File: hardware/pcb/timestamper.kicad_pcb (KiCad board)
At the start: 2 copper layers, 75 x 100 mm, 114 parts, among them J1 Conn_Coaxial, J2 Conn_Coaxial, J3 Conn_Coaxial, J4 JTAG, J5 ISP, J6 Conn_Coaxial, J7 USB_B_Micro, U1 AP1117-33, U10 ATMEGA328-AU, U11 74HC04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

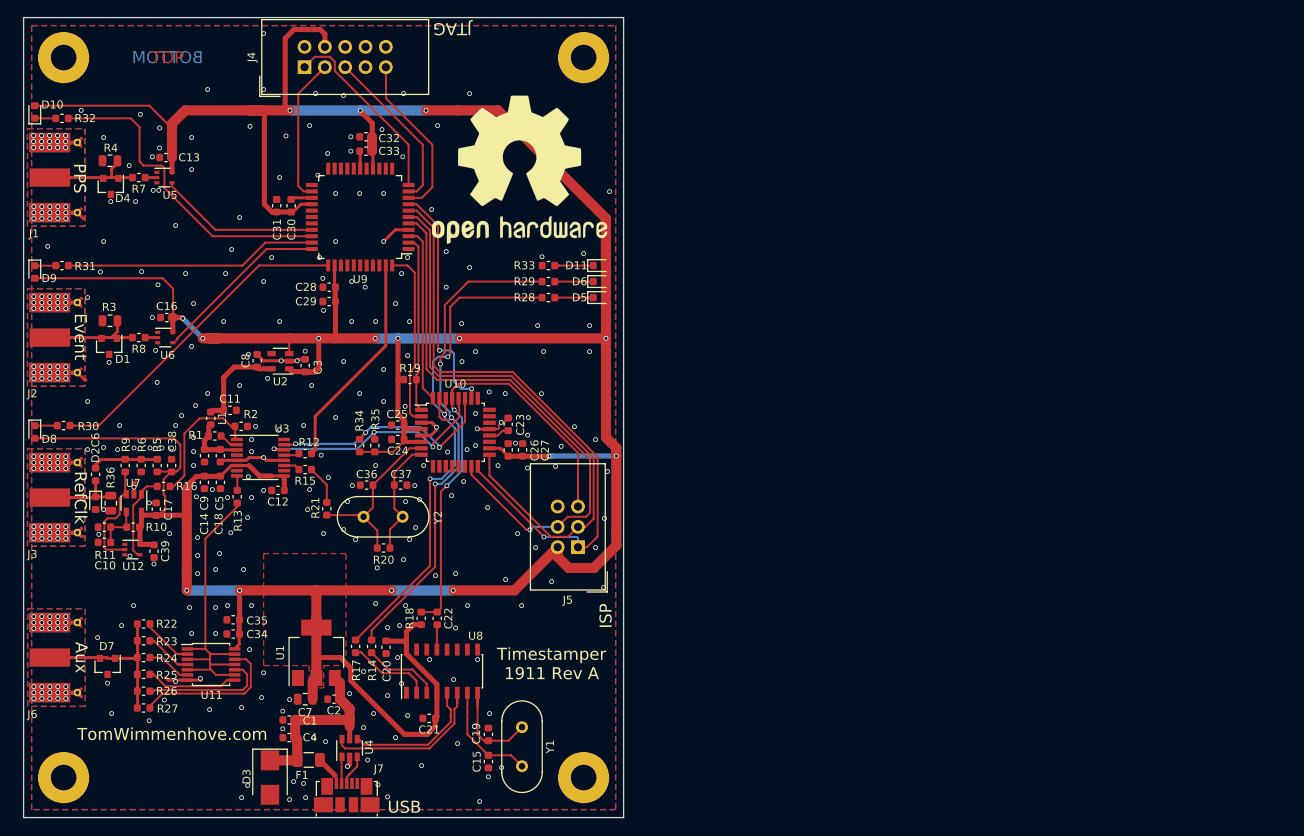
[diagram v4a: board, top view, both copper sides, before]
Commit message: Ground via insanity reduction
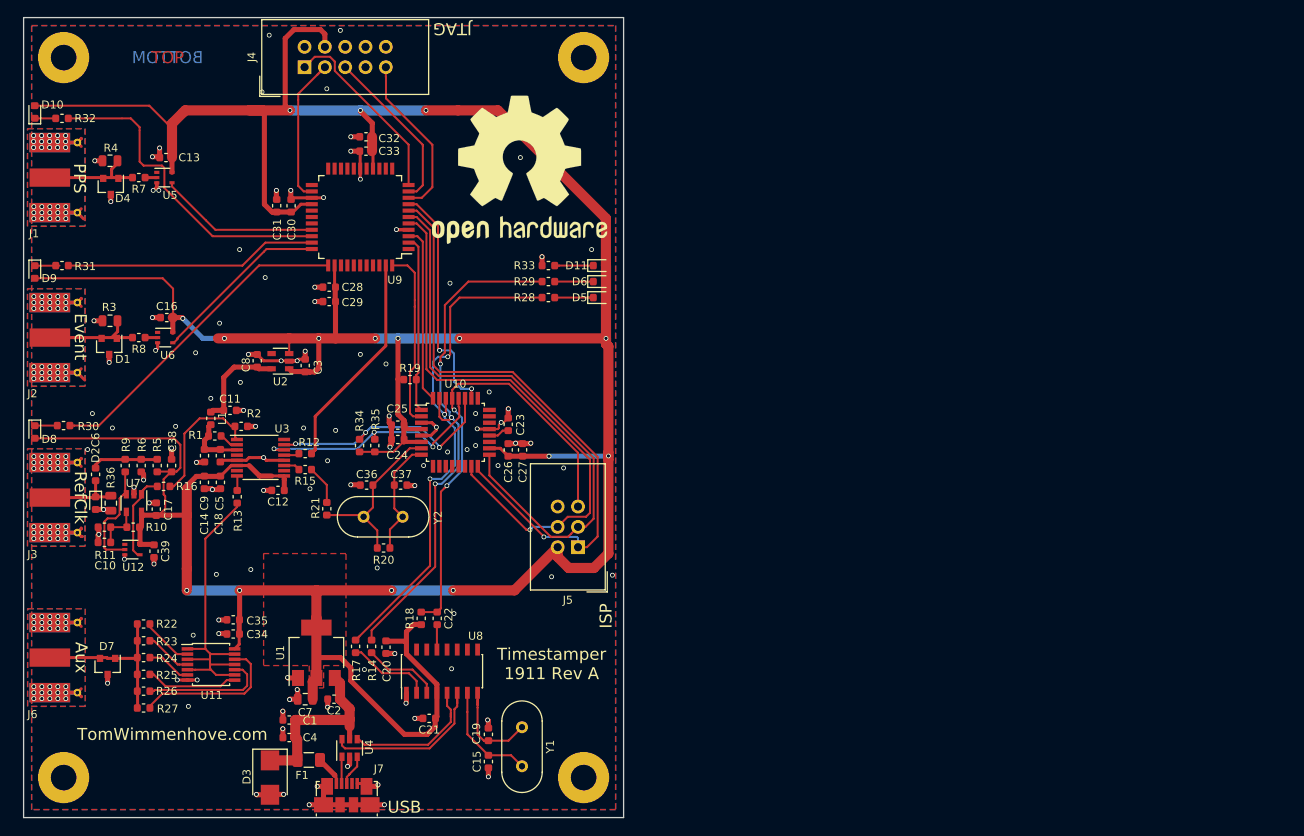
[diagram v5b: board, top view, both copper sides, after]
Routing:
- net GND: track 55.2 -> 133.9 mm, vias 371 -> 232
- net +3V3: track 516.2 -> 514.0 mm

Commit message: VCC plane on top
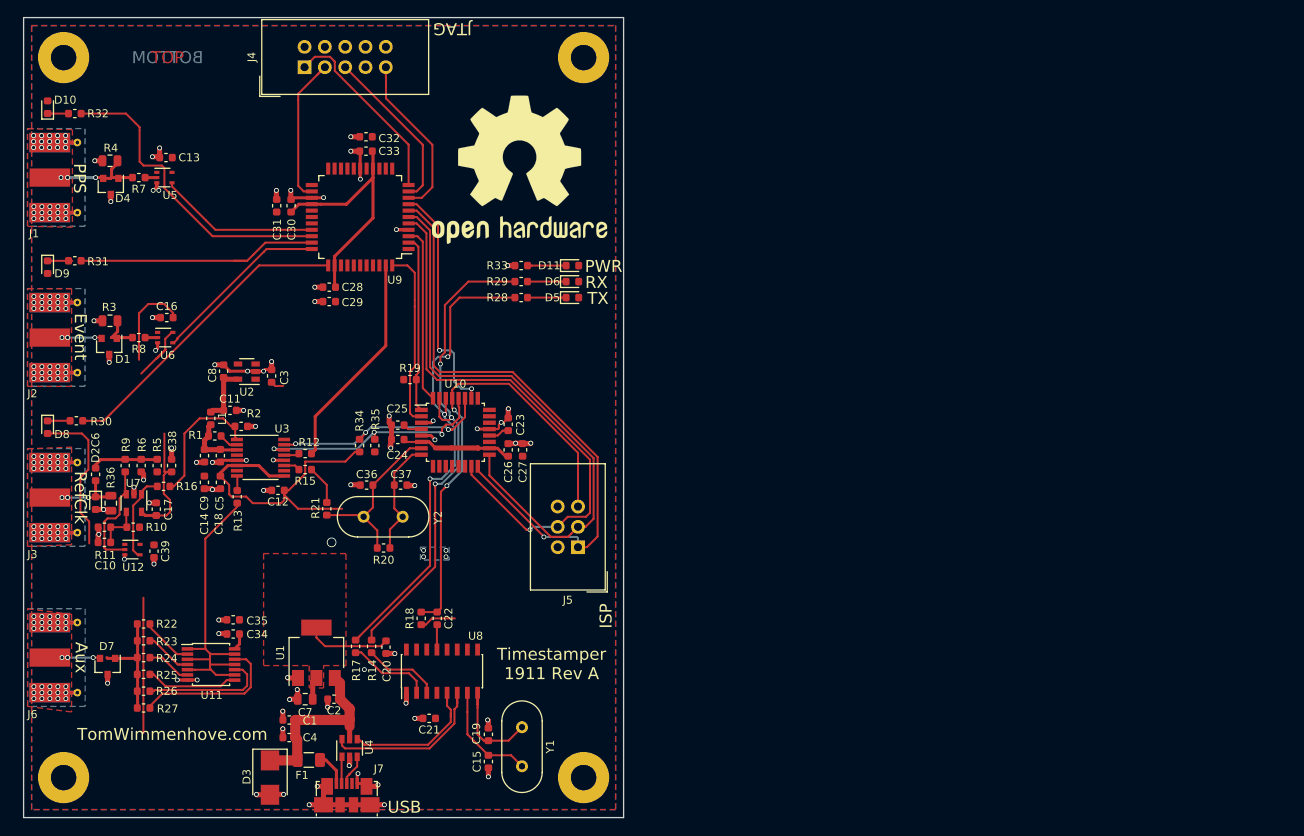
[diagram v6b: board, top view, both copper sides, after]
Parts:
- moved C3 4.40 mm to (81.0, 94.8)
- moved C8 4.40 mm to (75.0, 94.2)
- moved U2 4.40 mm to (77.9, 94.2)
- moved D11 3.40 mm to (118.6, 81.0)
- moved D5 3.40 mm to (118.6, 85.0)
- moved D6 3.40 mm to (118.6, 83.0)
- moved R28 3.40 mm to (112.2, 85.0)
- moved R29 3.40 mm to (112.2, 83.0)
- moved R33 3.40 mm to (112.2, 81.0)
- moved R32 1.71 mm to (56.4, 62.0)
- moved D10 1.71 mm to (53.0, 61.2)
- moved D8 1.71 mm to (53.0, 101.2)
- moved D9 1.71 mm to (53.0, 81.2)
- moved R30 1.71 mm to (56.6, 100.4)
- moved R31 1.71 mm to (56.4, 80.4)
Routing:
- net +3V3: track 514.0 -> 186.0 mm, vias 16 -> 4
- net GND: track 133.9 -> 119.8 mm, vias 232 -> 197
- net +1V8: track 12.4 -> 7.72 mm
- net /USBUART_RX: track 65.6 -> 62.2 mm
- net /USBUART_TX: track 64.4 -> 61.0 mm
- net Net-(D1-Pad1): track 12.8 -> 10.1 mm, vias 0 -> 3
- net /SDA: track 30.4 -> 27.9 mm
- net Net-(D7-Pad1): track 21.6 -> 19.2 mm, vias 0 -> 3
- net Net-(F1-Pad2): track 3.88 -> 5.24 mm
- net /LED_D10: track 40.6 -> 39.2 mm
- net Net-(C6-Pad2): track 9.68 -> 8.35 mm, vias 0 -> 3
- net Net-(D4-Pad1): track 14.2 -> 12.9 mm, vias 0 -> 3
- net /CPLD_HB: track 40.6 -> 39.3 mm
- net /SCL: track 31.2 -> 30.1 mm
- added copper zone on B.Cu, net +3V3
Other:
- board text added: "PWR"
- board text added: "RX"
- board text added: "TX"

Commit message: Small fixes
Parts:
- added C40: 0, Capacitor_SMD:C_0603_1608Metric, F.Cu at (94.5, 83.3)
- U12, U5, U6: value 74AHC1G14 -> 74LVC1G14
- moved R32 1.60 mm to (56.4, 60.4)
- moved C21 1.22 mm to (100.9, 136.4)
- moved C20 0.92 mm to (95.9, 129.4)
- moved D11 0.80 mm to (117.8, 81.0)
- moved D5 0.80 mm to (117.8, 85.0)
- moved D6 0.80 mm to (117.8, 83.0)
- moved R28 0.80 mm to (111.4, 85.0)
- moved R29 0.80 mm to (111.4, 83.0)
- moved R33 0.80 mm to (111.4, 81.0)
- moved C28 0.51 mm to (88.1, 83.2)
- moved C29 0.51 mm to (88.1, 85.0)
- moved C30 0.50 mm to (83.8, 73.2)
- moved C31 0.50 mm to (82.0, 73.2)
- turned D10 to 270 degrees
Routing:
- net GND: track 119.8 -> 110.5 mm, vias 197 -> 199
- net +3V3: track 186.0 -> 194.6 mm
- net /LED_D10: track 39.2 -> 40.8 mm
- net Net-(D1-Pad1): track 10.1 -> 11.1 mm
- net /SDA: track 27.9 -> 28.9 mm
- net Net-(D7-Pad1): track 19.2 -> 20.1 mm
- net /CPU_RST_N: track 57.9 -> 58.6 mm
- net /SCL: track 30.1 -> 30.7 mm
- net Net-(R14-Pad1): track 9.66 -> 10.2 mm

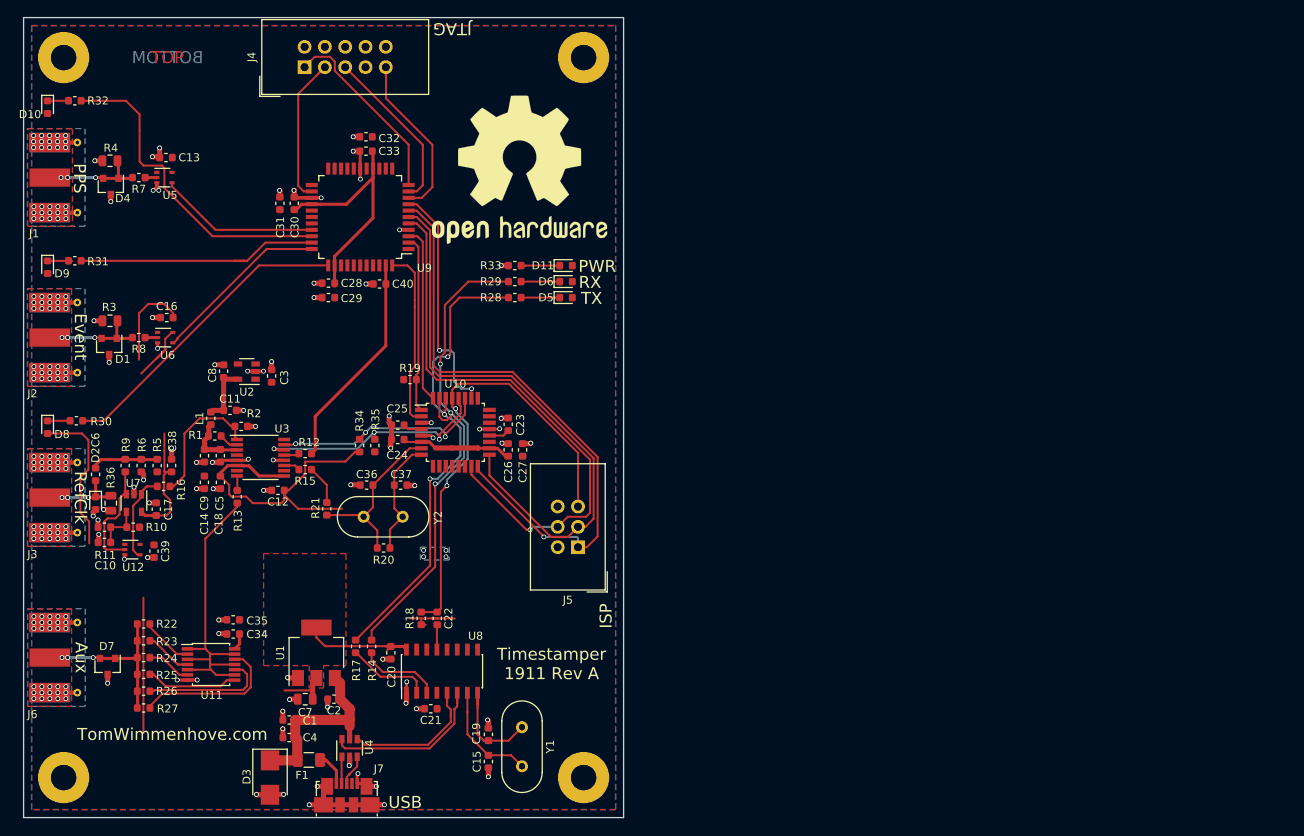
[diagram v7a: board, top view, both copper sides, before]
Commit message: Fixed mask clearance. Keep-out around mounting holes
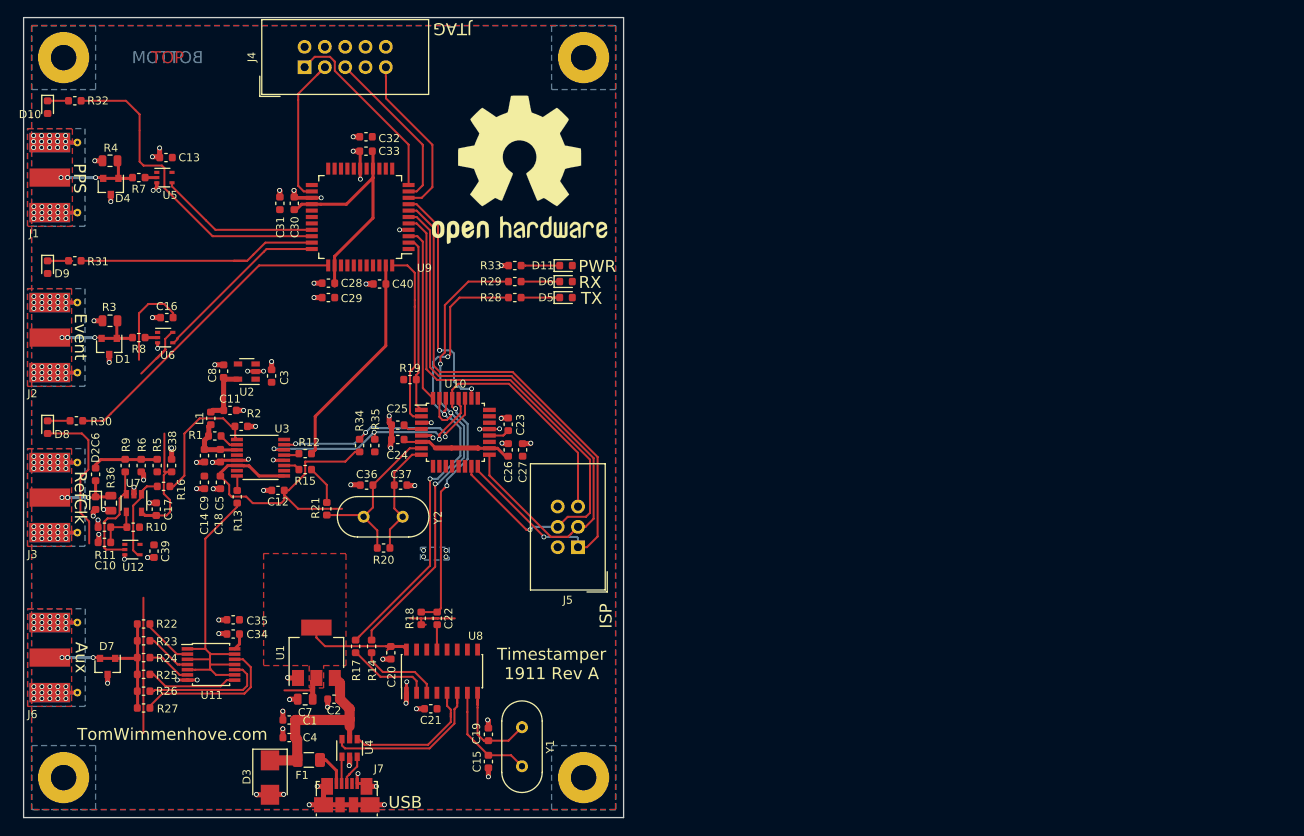
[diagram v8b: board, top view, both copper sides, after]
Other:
- rule pad_to_mask_clearance: 0.2 -> 0.075
- rule solder_mask_min_width: 0.25 -> 0.1
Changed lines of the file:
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@@
     (pad_size 0.9 0.8)
     (pad_drill 0)
-    (pad_to_mask_clearance 0.2)
-    (solder_mask_min_width 0.25)
+    (pad_to_mask_clearance 0.075)
+    (solder_mask_min_width 0.1)
     (aux_axis_origin 0 0)
     (visible_elements FFFEFF7F)
@@
       )
     )
+  )
+  (zone (net 0) (net_name "") (layer F.Cu) (hatch edge 0.508)
+    (connect_pads (clearance 0.3048))
+    (min_thickness 0.254)
+    (keepout (tracks allowed) (vias allowed) (copperpour not_allowed))
+    (fill (arc_segments 32) (thermal_gap 0.508) (thermal_bridge_width 0.508) (smoothing fillet) (radius 1))
+    (polygon
+      (pts
+        (xy 124 149) (xy 124 141) (xy 116 141) (xy 116 149)
+      )
+    )
+  )
+  (zone (net 0) (net_name "") (layer F.Cu) (hatch edge 0.508)
+    (connect_pads (clearance 0.3048))
+    (min_thickness 0.254)
+    (keepout (tracks allowed) (vias allowed) (copperpour not_allowed))
+    (fill (arc_segments 32) (thermal_gap 0.508) (thermal_bridge_width 0.508))
+    (polygon
+      (pts
+        (xy 59 149) (xy 59 141) (xy 51 141) (xy 51 148.947066)
+      )
+    )
+  )
+  (zone (net 0) (net_name "") (layer F.Cu) (hatch edge 0.508)
+    (connect_pads (clearance 0.3048))
+    (min_thickness 0.254)
+    (keepout (tracks allowed) (vias allowed) (copperpour not_allowed))
+    (fill (arc_segments 32) (thermal_gap 0.508) (thermal_bridge_width 0.508))
+    (polygon
+      (pts
+        (xy 124 59) (xy 124 51) (xy 116 51) (xy 116 59)
+      )
+    )
+  )
+  (zone (net 0) (net_name "") (layer F.Cu) (hatch edge 0.508)
+    (connect_pads (clearance 0.3048))
+    (min_thickness 0.254)
+    (keepout (tracks allowed) (vias allowed) (copperpour not_allowed))
+    (fill (arc_segments 32) (thermal_gap 0.508) (thermal_bridge_width 0.508))
+    (polygon
+      (pts
+        (xy 59 59) (xy 59 51) (xy 51 51) (xy 51 59)
+      )
+    )
+  )
+  (zone (net 1) (net_name GND) (layer B.Cu) (hatch edge 0.508)
+    (priority 1)
+    (connect_pads yes (clearance 0.3048))
+    (min_thickness 0.254)
+    (fill yes (arc_segments 32) (thermal_gap 0.508) (thermal_bridge_width 0.508))
+    (polygon
+      (pts
+        (xy 51 149) (xy 51 141) (xy 59 141) (xy 59 149)
+      )
+    )
+  )
+  (zone (net 1) (net_name GND) (layer B.Cu) (hatch edge 0.508)
+    (priority 1)
+    (connect_pads yes (clearance 0.3048))
+    (min_thickness 0.254)
+    (fill yes (arc_segments 32) (thermal_gap 0.508) (thermal_bridge_width 0.508))
+    (polygon
+      (pts
+        (xy 116 149) (xy 116 141) (xy 124 141) (xy 124 149)
+      )
+    )
+  )
+  (zone (net 1) (net_name GND) (layer B.Cu) (hatch edge 0.508)
+    (priority 1)
+    (connect_pads yes (clearance 0.3048))
+    (min_thickness 0.254)
+    (fill yes (arc_segments 32) (thermal_gap 0.508) (thermal_bridge_width 0.508))
+    (polygon
+      (pts
+        (xy 116 59) (xy 116 51) (xy 124 51) (xy 124 59)
+      )
+    )
+  )
+  (zone (net 1) (net_name GND) (layer B.Cu) (hatch edge 0.508)
+    (priority 1)
+    (connect_pads yes (clearance 0.3048))
+    (min_thickness 0.254)
+    (fill yes (arc_segments 32) (thermal_gap 0.508) (thermal_bridge_width 0.508))
+    (polygon
+      (pts
+        (xy 51 59) (xy 51 51) (xy 59 51) (xy 59 59)
+      )
+    )
